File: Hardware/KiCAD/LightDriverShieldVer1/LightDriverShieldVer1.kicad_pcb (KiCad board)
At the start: 2 copper layers, 25 parts, among them J1 Conn_01x12, J2 Conn_01x12, J3 Conn_01x06, J4 Screw_Terminal_01x04, J5 ExtVCC, Q1 2N3904, Q2 Si2301, Q3 2N3904, Q4 2N3904, Q5 2N3904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

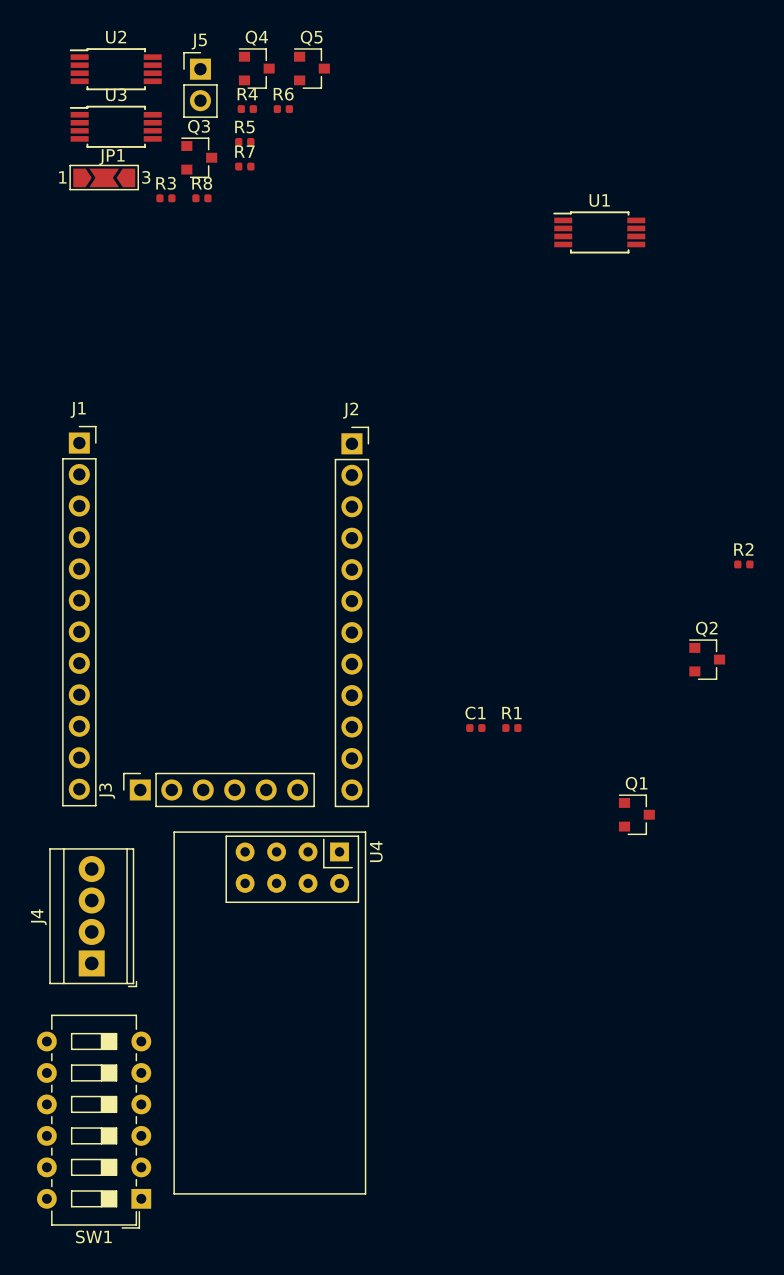
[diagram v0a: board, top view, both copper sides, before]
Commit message: Routed the shield for version 1
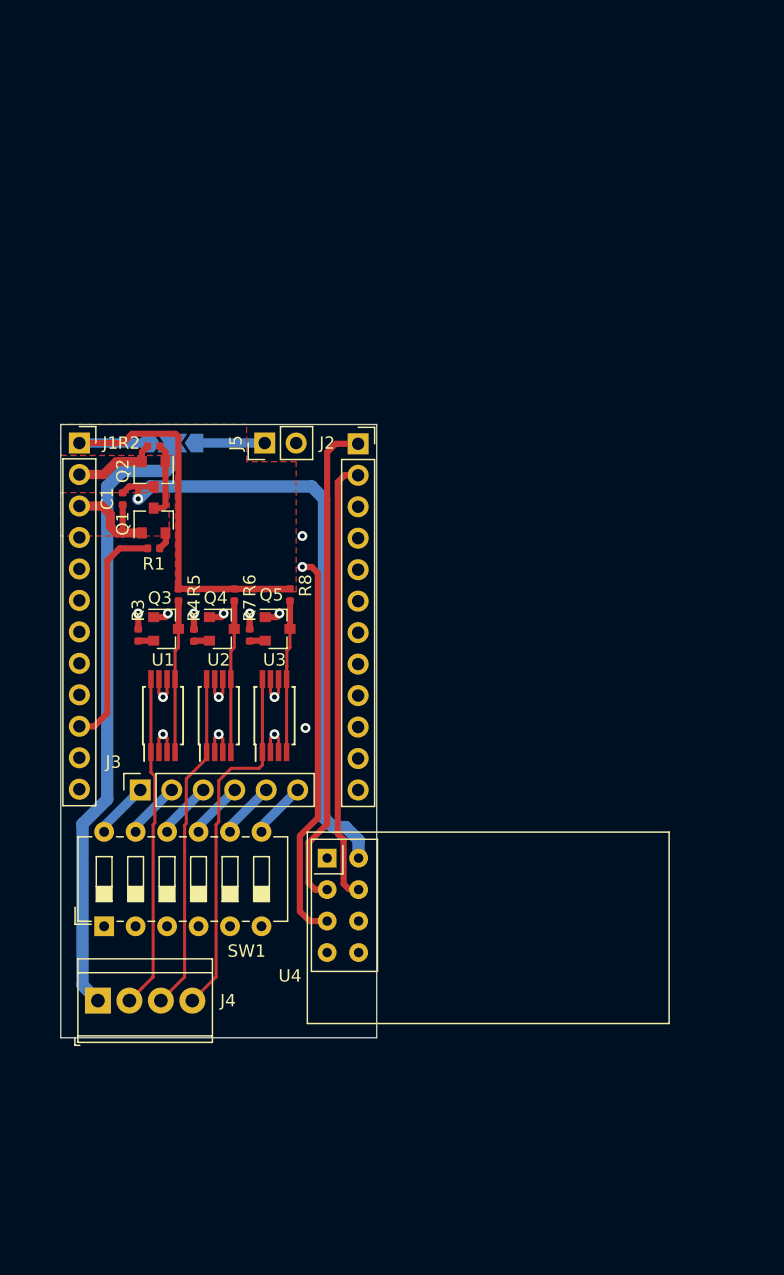
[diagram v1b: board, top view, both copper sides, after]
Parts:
- C1: value C_Small -> 1uF
- JP1: moved to B.Cu
- moved U2 52.8 mm to (111.2, 114.0), turned to 90 degrees
- moved U1 52.6 mm to (106.8, 114.0), turned to 90 degrees
- moved U3 49.2 mm to (115.8, 114.0), turned to 90 degrees
- moved R2 48.6 mm to (106.0, 92.2), turned to 180 degrees
- moved Q2 47.1 mm to (106.0, 94.5), turned to 270 degrees
- moved Q1 45.7 mm to (106.0, 98.2), turned to 90 degrees
- moved Q4 45.3 mm to (111.5, 107.0)
- moved Q5 45.3 mm to (116.0, 107.0)
- moved R4 42.7 mm to (109.2, 107.5), turned to 270 degrees
- moved R6 39.4 mm to (112.5, 104.2), turned to 90 degrees
- moved Q3 38.1 mm to (107.0, 107.0)
- moved R7 37.8 mm to (113.8, 107.5), turned to 270 degrees
- moved R5 36.9 mm to (108.0, 104.2), turned to 90 degrees
- moved R3 35.3 mm to (104.8, 107.5), turned to 270 degrees
- moved C1 34.0 mm to (103.5, 96.5), turned to 270 degrees
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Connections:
- J4 pad 2: (no net) -> DRV0
- SW1 pad 1: Net-(J3-Pad1) -> GND
- SW1 pad 10: GND -> Net-(J3-Pad3)
- SW1 pad 11: GND -> Net-(J3-Pad2)
- SW1 pad 12: GND -> Net-(J3-Pad1)
- SW1 pad 2: Net-(J3-Pad2) -> GND
- SW1 pad 3: Net-(J3-Pad3) -> GND
- SW1 pad 4: Net-(J3-Pad4) -> GND
- SW1 pad 5: Net-(J3-Pad5) -> GND
- SW1 pad 6: Net-(J3-Pad6) -> GND
- SW1 pad 7: GND -> Net-(J3-Pad6)
- SW1 pad 8: GND -> Net-(J3-Pad5)
- SW1 pad 9: GND -> Net-(J3-Pad4)
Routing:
- net VCCO: track 0.00 -> 50.6 mm
- net Net-(C1-Pad1): track 0.00 -> 50.3 mm, vias 0 -> 1
- net MISO: track 0.00 -> 41.4 mm, vias 0 -> 1
- net CE: track 0.00 -> 39.9 mm
- net SCK: track 0.00 -> 36.5 mm, vias 0 -> 1
- net CS: track 0.00 -> 35.9 mm
- net MOSI: track 0.00 -> 35.4 mm
- net OUT2: track 0.00 -> 35.4 mm, vias 0 -> 1
- net +5V: track 0.00 -> 35.2 mm
- net GND: track 0.00 -> 31.8 mm, vias 0 -> 9
- net IRQ: track 0.00 -> 30.6 mm, vias 0 -> 1
- net DRV2: track 0.00 -> 29.6 mm
- net DRV1: track 0.00 -> 27.5 mm
- net DRV0: track 0.00 -> 26.9 mm
- net OUT3: track 0.00 -> 25.8 mm, vias 0 -> 1
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- added copper zone on F.Cu, net +5V
- added copper zone on F.Cu, net GND
- added copper zone on In2.Cu, net GND
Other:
- board outline added: 25.5 x 49.5 mm
- copper layers 2 -> 4
- net class Signal added: clearance 0.2, trace_width 0.381, via_dia 0.45, via_drill 0.2
- rule pad_to_mask_clearance: 0.051 -> 0
- rule via_min_drill: 0.3 -> 0.2
- rule via_min_size: 0.4 -> 0.45

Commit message: Shield version 1 ordered.
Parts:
- added OUT0: TestPoint_Keystone_5015_Micro-Minature, TestPoint:TestPoint_Keystone_5015_Micro-Minature, B.Cu at (105.0, 114.0)
- added OUT1: TestPoint_Keystone_5015_Micro-Minature, TestPoint:TestPoint_Keystone_5015_Micro-Minature, B.Cu at (109.5, 114.0)
- added OUT2: TestPoint_Keystone_5015_Micro-Minature, TestPoint:TestPoint_Keystone_5015_Micro-Minature, B.Cu at (114.0, 114.0)
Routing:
- net DRV2: track 29.6 -> 30.4 mm, vias 0 -> 3
- net DRV0: track 26.9 -> 27.7 mm, vias 0 -> 3
- net DRV1: track 27.5 -> 28.3 mm, vias 0 -> 3
- added copper zone on F.Cu, net DRV0
- added copper zone on F.Cu, net DRV1
- added copper zone on F.Cu, net DRV2
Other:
- board text added: "0"
- board text added: "1"
- board text added: "EXT_+5V"
- board text added: "INT_+5V"
- board text added: "Node Address Select"
- board text added: "OUT0"
- board text added: "OUT1"
- board text added: "OUT2"
- board text added: "VCCO"
